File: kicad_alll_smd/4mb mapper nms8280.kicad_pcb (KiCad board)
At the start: 2 copper layers, 102.2 x 68.2 mm, 28 parts, among them IC131 74LS125, IC131B1 74LS125, IC131C1 74LS125, IC147 74LS157, IC147B1 74LS157, IC149 74LS670, IC149B1 74LS670, IC157B1 74LS08, IC180B1 74LS00, J1 Conn_01x10_Pin, U1 HY5117404B, U2 HY5117404B

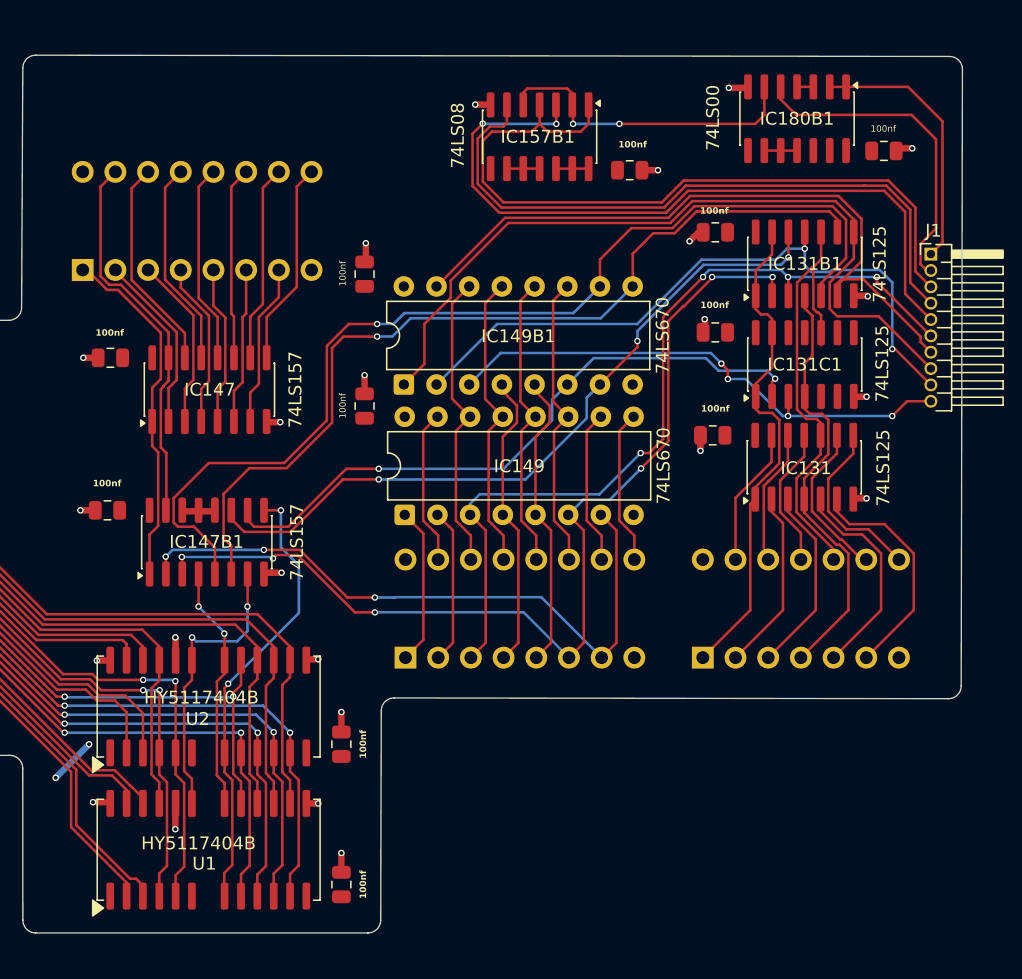
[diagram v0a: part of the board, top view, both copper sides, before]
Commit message: Publish 4 MB mapper project
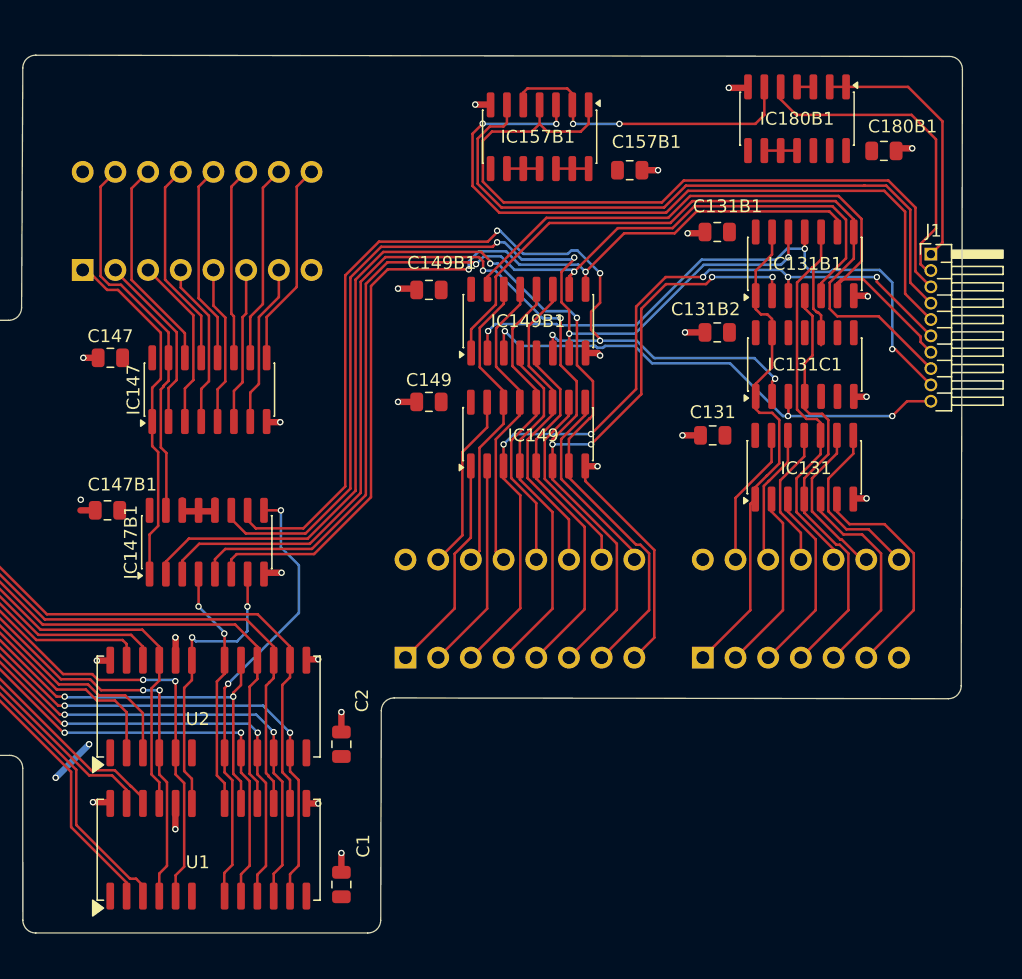
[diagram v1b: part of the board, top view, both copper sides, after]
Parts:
- IC149, IC149B1: footprint Package_DIP:DIP-16_W7.62mm -> Package_SO:SOIC-16_3.9x9.9mm_P1.27mm
- moved IC149 11.5 mm to (166.5, 92.4)
- moved IC149B1 10.9 mm to (166.5, 83.6)
- moved C149B1 5.15 mm to (158.8, 81.2), turned to 180 degrees
- moved C149 5.01 mm to (158.8, 89.9), turned to 180 degrees
- moved C131B1 0.15 mm to (181.2, 76.7)
- moved C131B2 0.15 mm to (181.2, 84.5)
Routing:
- net /4mb mapper nms8280/IC149_P7: track 51.1 -> 87.5 mm, vias 3 -> 2
- net /4mb mapper nms8280/IC149_P6: track 78.0 -> 112.2 mm
- net Net-(IC131C1-1D): track 51.2 -> 77.5 mm, vias 2 -> 5
- net GND: track 31.1 -> 51.8 mm, vias 24 -> 26
- net Net-(IC131B1-4D): track 57.6 -> 77.7 mm, vias 3 -> 4
- net Net-(IC131B1-3O): track 61.6 -> 55.1 mm
- net /4mb mapper nms8280/IC149_P5_IC149B: track 23.1 -> 29.3 mm
- net Net-(IC131B1-3D): track 69.4 -> 74.1 mm, vias 1 -> 2
- net /4mb mapper nms8280/IC149_P1: track 12.3 -> 17.0 mm
- net /4mb mapper nms8280/IC149_P4_IC149B: track 23.1 -> 27.8 mm
- net /4mb mapper nms8280/IC149_P2: track 12.1 -> 16.5 mm
- net Net-(IC131B1-4O): track 52.5 -> 48.6 mm, vias 2 -> 3
- net /4mb mapper nms8280/IC149_P9: track 12.0 -> 15.4 mm
- net Net-(IC131B1-2O): track 54.4 -> 51.1 mm
- net /4mb mapper nms8280/IC149_P10: track 12.0 -> 14.8 mm
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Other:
- board text removed: "J1 - to IC180 pin 12 J2 - to R130 J3 - to IC111 pin 2 J4 - to R127 J5 - to R128 J6 - to IC161 pin 11 J7 - to IC176 pin 11 J8 - to IC176 pin 13 J9 - to IC178 pin 5 J10 - to IC178 pin 7"
